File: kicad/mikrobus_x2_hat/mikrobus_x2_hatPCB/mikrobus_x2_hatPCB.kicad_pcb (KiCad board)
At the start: 2 copper layers, 65 x 56.5 mm, 7 parts, among them IC1 MIKROE-924, IC2 MIKROE-924, J1 RPi_GPIO

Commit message: PCB completed
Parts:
- moved IC1 0.87 mm to (124.6, 94.1)
- moved IC2 0.67 mm to (153.2, 94.1)
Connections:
- IC1 pad 1: unconnected-(IC1-AN-Pad1) -> Net-(IC1-AN)
- IC1 pad 10: unconnected-(IC1-INT-Pad10) -> Net-(IC1-INT)
- IC1 pad 11: unconnected-(IC1-RX-Pad11) -> Net-(IC1-RX)
- IC1 pad 12: unconnected-(IC1-TX-Pad12) -> Net-(IC1-TX)
- IC1 pad 13: unconnected-(IC1-SCL-Pad13) -> Net-(IC1-SCL)
- IC1 pad 14: unconnected-(IC1-SDA-Pad14) -> Net-(IC1-SDA)
- IC1 pad 15: unconnected-(IC1-+5V-Pad15) -> 5V
- IC1 pad 16: unconnected-(IC1-GND_2-Pad16) -> GND
- IC1 pad 2: unconnected-(IC1-RST-Pad2) -> Net-(IC1-RST)
- IC1 pad 3: unconnected-(IC1-CS-Pad3) -> Net-(IC1-CS)
- IC1 pad 4: unconnected-(IC1-SCK-Pad4) -> Net-(IC1-SCK)
- IC1 pad 5: unconnected-(IC1-MISO-Pad5) -> Net-(IC1-MISO)
- IC1 pad 6: unconnected-(IC1-MOSI-Pad6) -> Net-(IC1-MOSI)
- IC1 pad 7: unconnected-(IC1-+3.3V-Pad7) -> 3V3
- IC1 pad 8: unconnected-(IC1-GND_1-Pad8) -> GND
- IC1 pad 9: unconnected-(IC1-PWM-Pad9) -> Net-(IC1-PWM)
- IC2 pad 1: unconnected-(IC2-AN-Pad1) -> Net-(IC2-AN)
- IC2 pad 10: unconnected-(IC2-INT-Pad10) -> Net-(IC2-INT)
- IC2 pad 11: unconnected-(IC2-RX-Pad11) -> Net-(IC1-RX)
- IC2 pad 12: unconnected-(IC2-TX-Pad12) -> Net-(IC1-TX)
- IC2 pad 13: unconnected-(IC2-SCL-Pad13) -> Net-(IC1-SCL)
- IC2 pad 14: unconnected-(IC2-SDA-Pad14) -> Net-(IC1-SDA)
- IC2 pad 15: unconnected-(IC2-+5V-Pad15) -> 5V
- IC2 pad 16: unconnected-(IC2-GND_2-Pad16) -> GND
- IC2 pad 2: unconnected-(IC2-RST-Pad2) -> Net-(IC2-RST)
- IC2 pad 3: unconnected-(IC2-CS-Pad3) -> Net-(IC2-CS)
- IC2 pad 4: unconnected-(IC2-SCK-Pad4) -> Net-(IC1-SCK)
- IC2 pad 5: unconnected-(IC2-MISO-Pad5) -> Net-(IC1-MISO)
- IC2 pad 6: unconnected-(IC2-MOSI-Pad6) -> Net-(IC1-MOSI)
- IC2 pad 7: unconnected-(IC2-+3.3V-Pad7) -> 3V3
- IC2 pad 8: unconnected-(IC2-GND_1-Pad8) -> GND
- IC2 pad 9: unconnected-(IC2-PWM-Pad9) -> Net-(IC2-PWM)
- J1 pad 1: unconnected-(J1-3.3V-Pad1) -> 3V3
- J1 pad 10: unconnected-(J1-BCM15_RXD-Pad10) -> Net-(IC1-RX)
- J1 pad 11: unconnected-(J1-BCM17-Pad11) -> Net-(IC2-PWM)
- J1 pad 12: unconnected-(J1-BCM18_PCM_C-Pad12) -> Net-(IC1-PWM)
- J1 pad 14: unconnected-(J1-GND-Pad14) -> GND
- J1 pad 17: unconnected-(J1-3.3V-Pad17) -> 3V3
- J1 pad 19: unconnected-(J1-BCM10_MOSI-Pad19) -> Net-(IC1-MOSI)
- J1 pad 2: unconnected-(J1-5V-Pad2) -> 5V
- J1 pad 20: unconnected-(J1-GND-Pad20) -> GND
- J1 pad 21: unconnected-(J1-BCM9_MISO-Pad21) -> Net-(IC1-MISO)
- J1 pad 23: unconnected-(J1-BCM11_SCLK-Pad23) -> Net-(IC1-SCK)
- J1 pad 24: unconnected-(J1-BCM8_CE0-Pad24) -> Net-(IC1-CS)
- J1 pad 25: unconnected-(J1-GND-Pad25) -> GND
- J1 pad 26: unconnected-(J1-BCM7_CE1-Pad26) -> Net-(IC2-CS)
- J1 pad 29: unconnected-(J1-BCM5-Pad29) -> Net-(IC1-RST)
- J1 pad 3: unconnected-(J1-BCM2_SDA-Pad3) -> Net-(IC1-SDA)
- J1 pad 30: unconnected-(J1-GND-Pad30) -> GND
- J1 pad 31: unconnected-(J1-BCM6-Pad31) -> Net-(IC1-INT)
- J1 pad 33: unconnected-(J1-BCM13_PWM1-Pad33) -> Net-(IC2-AN)
- J1 pad 34: unconnected-(J1-GND-Pad34) -> GND
- J1 pad 35: unconnected-(J1-BCM19_MISO_PCM_FS-Pad35) -> Net-(IC2-RST)
- J1 pad 37: unconnected-(J1-BCM26-Pad37) -> Net-(IC2-INT)
- J1 pad 39: unconnected-(J1-GND-Pad39) -> GND
- J1 pad 4: unconnected-(J1-5V-Pad4) -> 5V
- J1 pad 5: unconnected-(J1-BCM3_SCL-Pad5) -> Net-(IC1-SCL)
- J1 pad 6: unconnected-(J1-GND-Pad6) -> GND
- J1 pad 7: unconnected-(J1-BCM4_GPCLK0-Pad7) -> Net-(IC1-AN)
- J1 pad 8: unconnected-(J1-BCM14_TXD-Pad8) -> Net-(IC1-TX)
- J1 pad 9: unconnected-(J1-GND-Pad9) -> GND
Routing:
- net 5V: track 0.00 -> 92.9 mm, vias 0 -> 2
- net 3V3: track 0.00 -> 87.0 mm, vias 0 -> 2
- net Net-(IC1-SDA): track 0.00 -> 70.9 mm, vias 0 -> 2
- net Net-(IC1-TX): track 0.00 -> 66.1 mm
- net Net-(IC1-SCL): track 0.00 -> 65.4 mm, vias 0 -> 2
- net Net-(IC1-RX): track 0.00 -> 62.5 mm
- net Net-(IC1-MOSI): track 0.00 -> 61.8 mm
- net Net-(IC1-MISO): track 0.00 -> 58.2 mm
- net Net-(IC1-SCK): track 0.00 -> 54.6 mm
- net Net-(IC2-PWM): track 0.00 -> 53.3 mm, vias 0 -> 3
- net Net-(IC1-RST): track 0.00 -> 42.6 mm, vias 0 -> 3
- net Net-(IC1-CS): track 0.00 -> 39.9 mm, vias 0 -> 1
- net Net-(IC2-CS): track 0.00 -> 28.6 mm
- net Net-(IC1-PWM): track 0.00 -> 26.9 mm
- net Net-(IC1-INT): track 0.00 -> 25.3 mm, vias 0 -> 1
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- added copper zone on F.Cu, net GND
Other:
- outline, holes or cut-outs redrawn

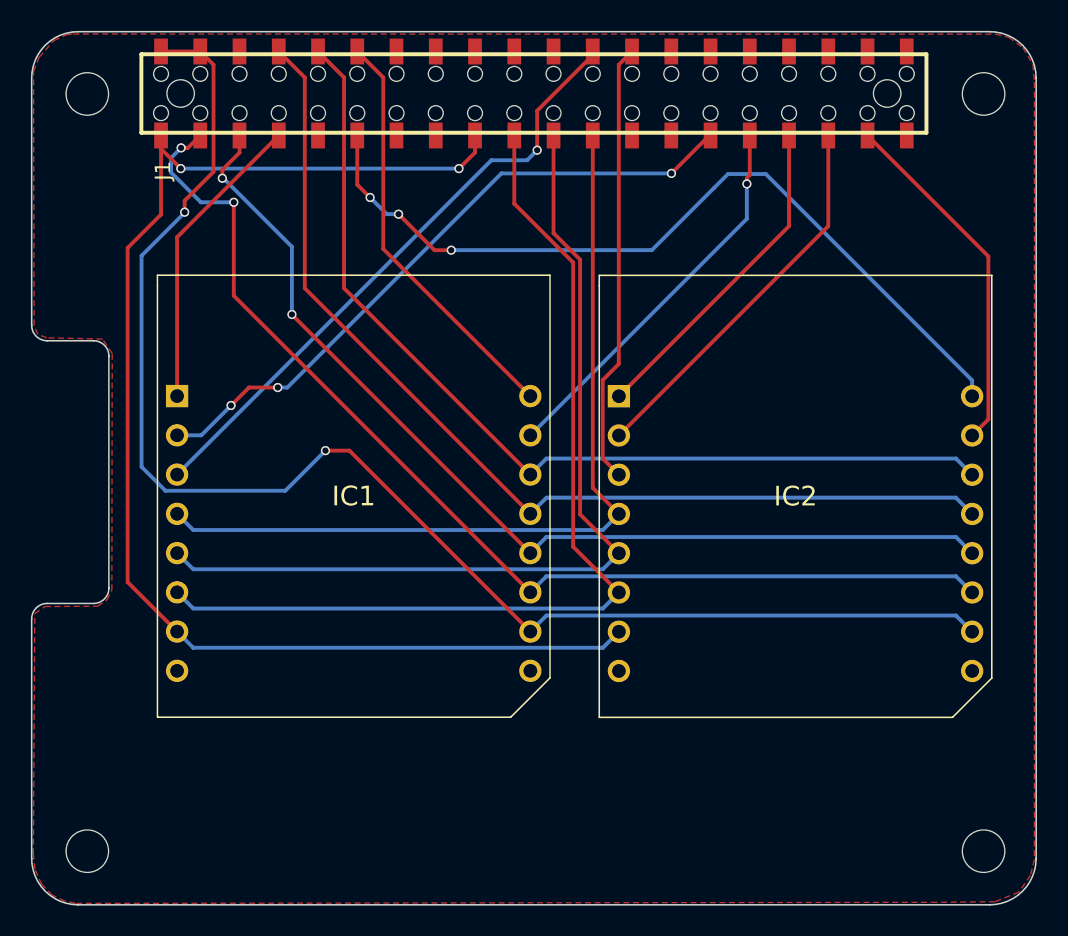
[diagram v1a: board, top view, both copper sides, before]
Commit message: MikroBUS logo added
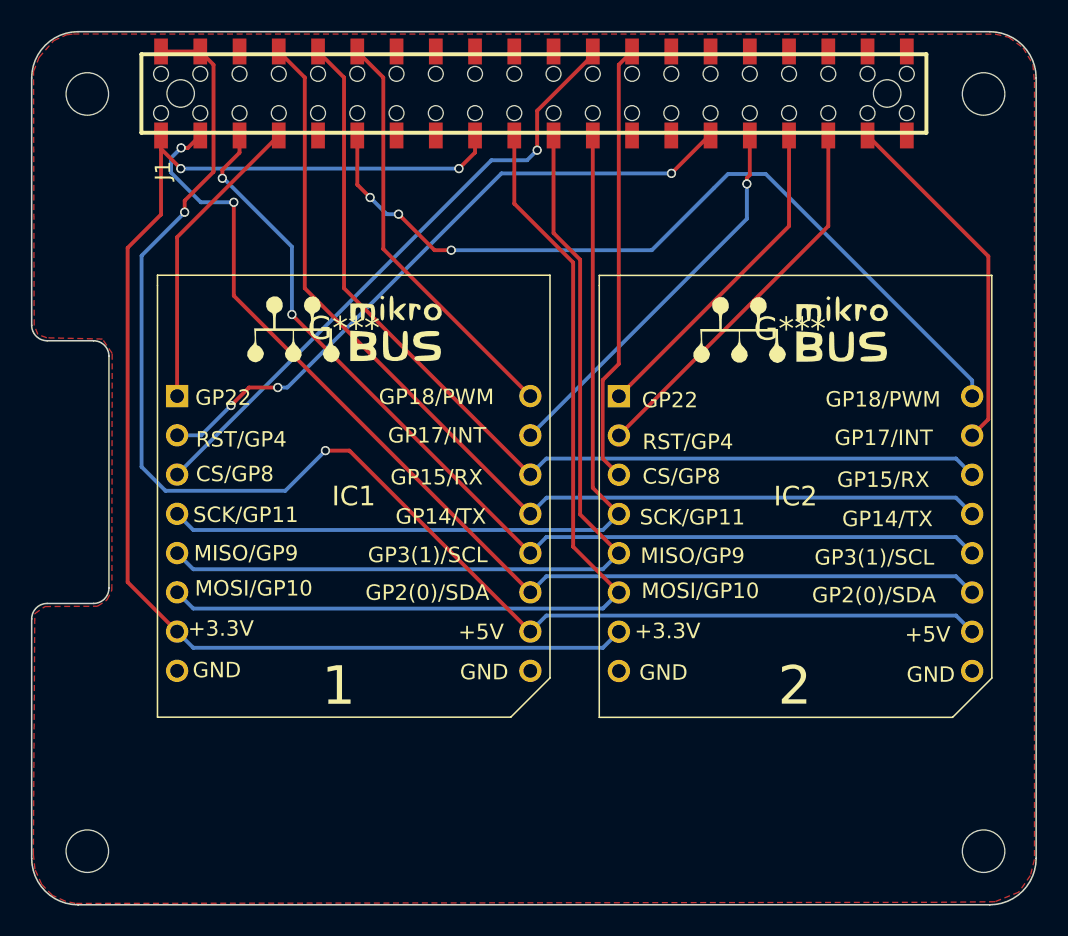
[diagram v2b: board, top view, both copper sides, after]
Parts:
- added G***: LOGO, logo:mikro_logo, F.Cu at (164.2, 89.8)
- added G***: LOGO, logo:mikro_logo, F.Cu at (135.4, 89.7)
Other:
- board text added: "+3.3V"
- board text added: "+5V"
- board text added: "1"
- board text added: "2"
- board text added: "CS/GP8"
- board text added: "GND"
- board text added: "GP14/TX"
- board text added: "GP15/RX"
- board text added: "GP17/INT"
- board text added: "GP18/PWM"
- board text added: "GP2(0)/SDA"
- board text added: "GP22"
- board text added: "GP3(1)/SCL"
- board text added: "MISO/GP9"
- board text added: "MOSI/GP10"
- board text added: "RST/GP4"
- board text added: "SCK/GP11"
